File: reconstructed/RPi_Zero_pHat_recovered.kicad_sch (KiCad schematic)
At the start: 6 parts, among them J1 RPi_GPIO, J2 Wind, J3 RainFall, U1 MCP3008, U2 BME280

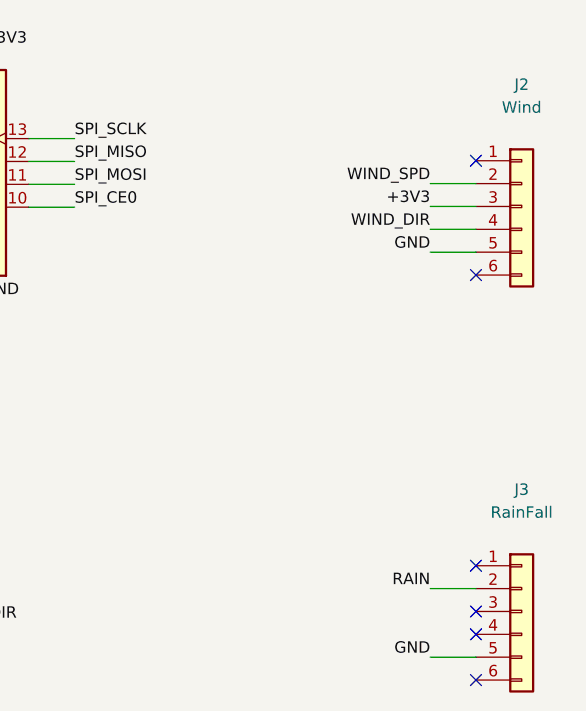
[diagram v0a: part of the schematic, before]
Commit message: Fix RJ jack pin numbering: pads are staggered, not row-major
The modular-jack footprint numbers pins across the connector (1.27mm in x)
with odd pins in one row and even in the other, not row-major. With the
correct numbering Wind lands on pins 2-5 (a 6P4C plug) and RainFall on the
centre pair 3-4 (6P2C) - contiguous, as real modular plugs require. The
previous numbering put +3V3 on the anemometer common, so a cable built from
it would have shorted 3V3 to ground.

Adds a jack pinout table to the README.
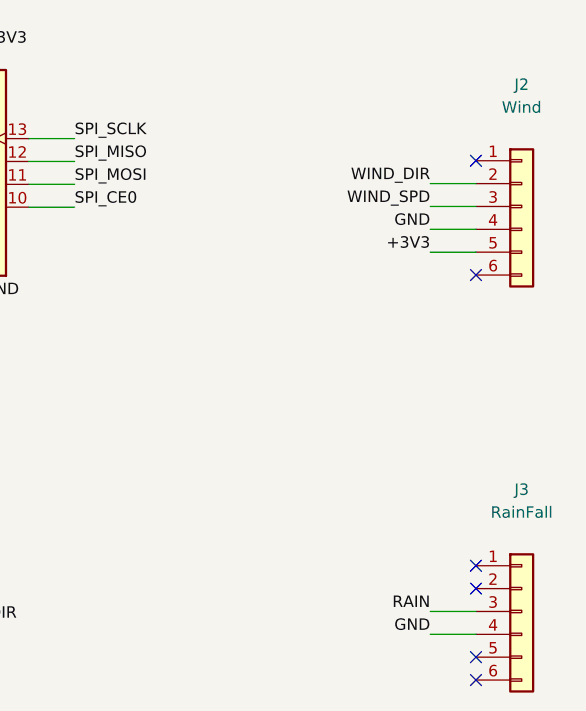
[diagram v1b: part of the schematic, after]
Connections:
- net +3V3: now also J2.5 (Pin_5); no longer J2.3 (Pin_3)
- net GND: now also J2.4 (Pin_4), J3.4 (Pin_4); no longer J2.5 (Pin_5), J3.5 (Pin_5)
- net RAIN: now also J3.3 (Pin_3); no longer J3.2 (Pin_2)
- net WIND_DIR: now also J2.2 (Pin_2); no longer J2.4 (Pin_4)
- net WIND_SPD: now also J2.3 (Pin_3); no longer J2.2 (Pin_2)
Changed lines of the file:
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@@
     (pin "9")
     (instances (project "RPi_Zero_pHat_recovered"
-      (path "/72064c25-0dc4-4eda-845f-894c0f4be2dc" (reference "J1") (unit 1))))
+      (path "/6ac0e1ad-4e39-4eb3-8b97-7b9d8c0f23c9" (reference "J1") (unit 1))))
   )
   (symbol (lib_id "Analog_ADC:MCP3008") (at 145 105 0) (unit 1)
@@
     (pin "9")
     (instances (project "RPi_Zero_pHat_recovered"
-      (path "/72064c25-0dc4-4eda-845f-894c0f4be2dc" (reference "U1") (unit 1))))
+      (path "/6ac0e1ad-4e39-4eb3-8b97-7b9d8c0f23c9" (reference "U1") (unit 1))))
   )
   (symbol (lib_id "Connector_Generic:Conn_01x07") (at 215 60 0) (unit 1)
@@
     (pin "7")
     (instances (project "RPi_Zero_pHat_recovered"
-      (path "/72064c25-0dc4-4eda-845f-894c0f4be2dc" (reference "U2") (unit 1))))
+      (path "/6ac0e1ad-4e39-4eb3-8b97-7b9d8c0f23c9" (reference "U2") (unit 1))))
   )
   (symbol (lib_id "Connector_Generic:Conn_01x06") (at 215 110 0) (unit 1)
@@
     (pin "6")
     (instances (project "RPi_Zero_pHat_recovered"
-      (path "/72064c25-0dc4-4eda-845f-894c0f4be2dc" (reference "J2") (unit 1))))
+      (path "/6ac0e1ad-4e39-4eb3-8b97-7b9d8c0f23c9" (reference "J2") (unit 1))))
   )
   (symbol (lib_id "Connector_Generic:Conn_01x06") (at 215 155 0) (unit 1)
@@
     (pin "6")
     (instances (project "RPi_Zero_pHat_recovered"
-      (path "/72064c25-0dc4-4eda-845f-894c0f4be2dc" (reference "J3") (unit 1))))
+      (path "/6ac0e1ad-4e39-4eb3-8b97-7b9d8c0f23c9" (reference "J3") (unit 1))))
   )
   (symbol (lib_id "Device:R") (at 145 160 0) (unit 1)
@@
     (pin "2")
     (instances (project "RPi_Zero_pHat_recovered"
-      (path "/72064c25-0dc4-4eda-845f-894c0f4be2dc" (reference "R1") (unit 1))))
+      (path "/6ac0e1ad-4e39-4eb3-8b97-7b9d8c0f23c9" (reference "R1") (unit 1))))
   )
   (wire (pts (xy 54.92 92.3) (xy 49.84 92.3)) (stroke (width 0) (type default)))
@@
   (wire (pts (xy 54.92 130.4) (xy 49.84 130.4)) (stroke (width 0) (type default)))
   (label "GND" (at 49.84 130.4 0) (fields_autoplaced yes) (effects (font (size 1.27 1.27)) (justify right bottom)))
-  (wire (pts (xy 209.92 115.08) (xy 204.83999999999997 115.08)) (stroke (width 0) (type default)))
-  (label "GND" (at 204.83999999999997 115.08 0) (fields_autoplaced yes) (effects (font (size 1.27 1.27)) (justify right bottom)))
-  (wire (pts (xy 209.92 160.08) (xy 204.83999999999997 160.08)) (stroke (width 0) (type default)))
-  (label "GND" (at 204.83999999999997 160.08 0) (fields_autoplaced yes) (effects (font (size 1.27 1.27)) (justify right bottom)))
+  (wire (pts (xy 209.92 112.54) (xy 204.83999999999997 112.54)) (stroke (width 0) (type default)))
+  (label "GND" (at 204.83999999999997 112.54 0) (fields_autoplaced yes) (effects (font (size 1.27 1.27)) (justify right bottom)))
+  (wire (pts (xy 209.92 157.54) (xy 204.83999999999997 157.54)) (stroke (width 0) (type default)))
+  (label "GND" (at 204.83999999999997 157.54 0) (fields_autoplaced yes) (effects (font (size 1.27 1.27)) (justify right bottom)))
   (wire (pts (xy 145.0 163.81) (xy 150.08 163.81)) (stroke (width 0) (type default)))
   (label "GND" (at 150.08 163.81 0) (fields_autoplaced yes) (effects (font (size 1.27 1.27)) (justify left bottom)))
@@
   (wire (pts (xy 54.92 102.46) (xy 49.84 102.46)) (stroke (width 0) (type default)))
   (label "+3V3" (at 49.84 102.46 0) (fields_autoplaced yes) (effects (font (size 1.27 1.27)) (justify right bottom)))
-  (wire (pts (xy 209.92 110.0) (xy 204.83999999999997 110.0)) (stroke (width 0) (type default)))
-  (label "+3V3" (at 204.83999999999997 110.0 0) (fields_autoplaced yes) (effects (font (size 1.27 1.27)) (justify right bottom)))
+  (wire (pts (xy 209.92 115.08) (xy 204.83999999999997 115.08)) (stroke (width 0) (type default)))
+  (label "+3V3" (at 204.83999999999997 115.08 0) (fields_autoplaced yes) (effects (font (size 1.27 1.27)) (justify right bottom)))
   (wire (pts (xy 142.46 92.3) (xy 137.38 92.3)) (stroke (width 0) (type default)))
   (label "+3V3" (at 137.38 92.3 0) (fields_autoplaced yes) (effects (font (size 1.27 1.27)) (justify right bottom)))
@@
   (wire (pts (xy 54.92 117.7) (xy 49.84 117.7)) (stroke (width 0) (type default)))
   (label "WIND_SPD" (at 49.84 117.7 0) (fields_autoplaced yes) (effects (font (size 1.27 1.27)) (justify right bottom)))
-  (wire (pts (xy 209.92 107.46) (xy 204.83999999999997 107.46)) (stroke (width 0) (type default)))
-  (label "WIND_SPD" (at 204.83999999999997 107.46 0) (fields_autoplaced yes) (effects (font (size 1.27 1.27)) (justify right bottom)))
+  (wire (pts (xy 209.92 110.0) (xy 204.83999999999997 110.0)) (stroke (width 0) (type default)))
+  (label "WIND_SPD" (at 204.83999999999997 110.0 0) (fields_autoplaced yes) (effects (font (size 1.27 1.27)) (justify right bottom)))
   (wire (pts (xy 54.92 120.24) (xy 49.84 120.24)) (stroke (width 0) (type default)))
   (label "RAIN" (at 49.84 120.24 0) (fields_autoplaced yes) (effects (font (size 1.27 1.27)) (justify right bottom)))
-  (wire (pts (xy 209.92 152.46) (xy 204.83999999999997 152.46)) (stroke (width 0) (type default)))
-  (label "RAIN" (at 204.83999999999997 152.46 0) (fields_autoplaced yes) (effects (font (size 1.27 1.27)) (justify right bottom)))
-  (wire (pts (xy 209.92 112.54) (xy 204.83999999999997 112.54)) (stroke (width 0) (type default)))
-  (label "WIND_DIR" (at 204.83999999999997 112.54 0) (fields_autoplaced yes) (effects (font (size 1.27 1.27)) (justify right bottom)))
+  (wire (pts (xy 209.92 155.0) (xy 204.83999999999997 155.0)) (stroke (width 0) (type default)))
+  (label "RAIN" (at 204.83999999999997 155.0 0) (fields_autoplaced yes) (effects (font (size 1.27 1.27)) (justify right bottom)))
+  (wire (pts (xy 209.92 107.46) (xy 204.83999999999997 107.46)) (stroke (width 0) (type default)))
+  (label "WIND_DIR" (at 204.83999999999997 107.46 0) (fields_autoplaced yes) (effects (font (size 1.27 1.27)) (justify right bottom)))
   (wire (pts (xy 145.0 156.19) (xy 150.08 156.19)) (stroke (width 0) (type default)))
   (label "WIND_DIR" (at 150.08 156.19 0) (fields_autoplaced yes) (effects (font (size 1.27 1.27)) (justify left bottom)))
@@
   (no_connect (at 209.92 117.62))
   (no_connect (at 209.92 149.92))
-  (no_connect (at 209.92 155.0))
-  (no_connect (at 209.92 157.54))
+  (no_connect (at 209.92 152.46))
+  (no_connect (at 209.92 160.08))
   (no_connect (at 209.92 162.62))
 )
